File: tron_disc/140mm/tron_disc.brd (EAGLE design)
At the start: 127 x 127 mm, 75 parts, among them IC1 SLICE_NOSHIFT_TLC5947HTSSOP32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, IC2 MEGA328-AI, IC3 SLICE_NOSHIFT_TLC5947HTSSOP32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, IC4 SLICE_NOSHIFT_TLC5947HTSSOP32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, X1 16Mhz

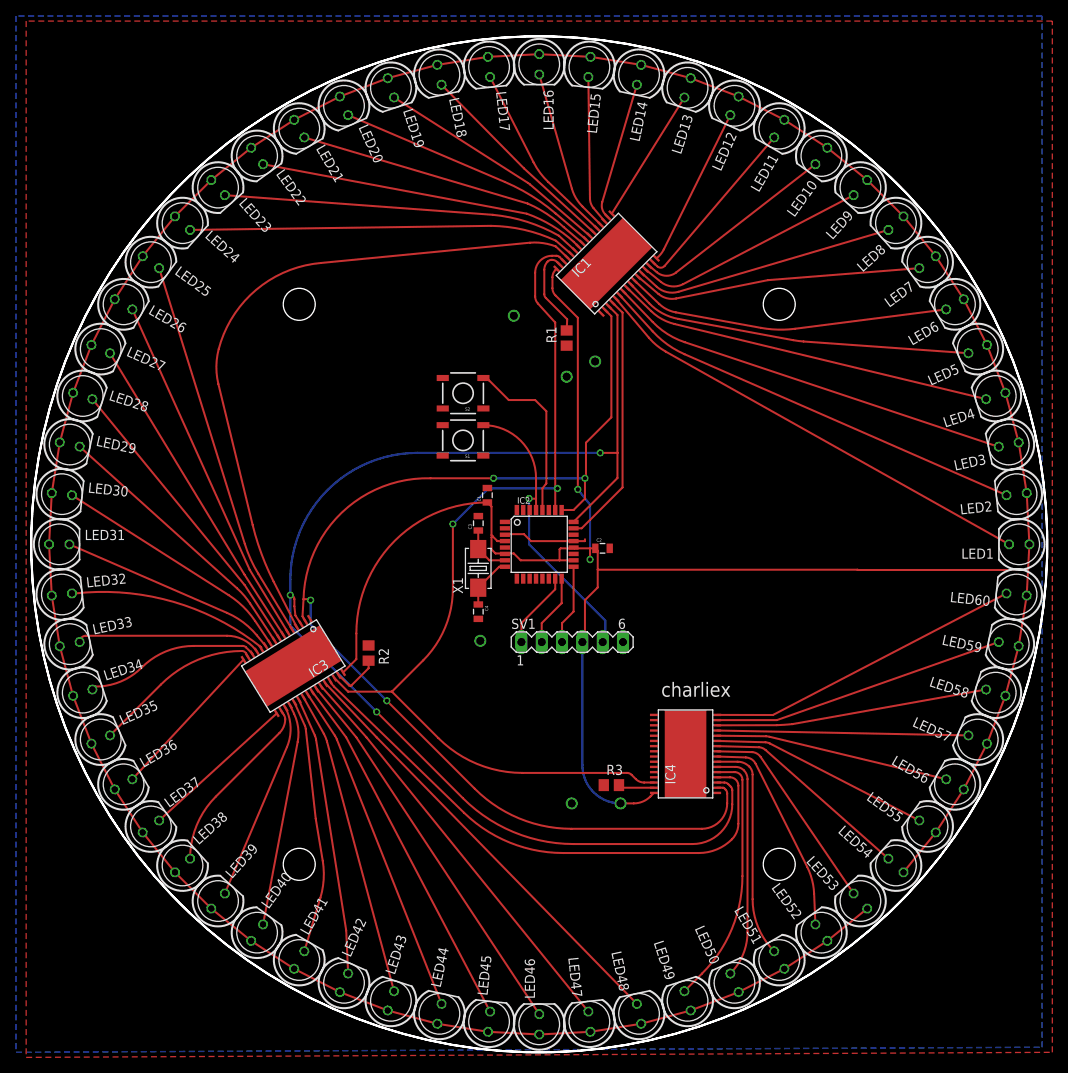
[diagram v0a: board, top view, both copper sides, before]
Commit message: 
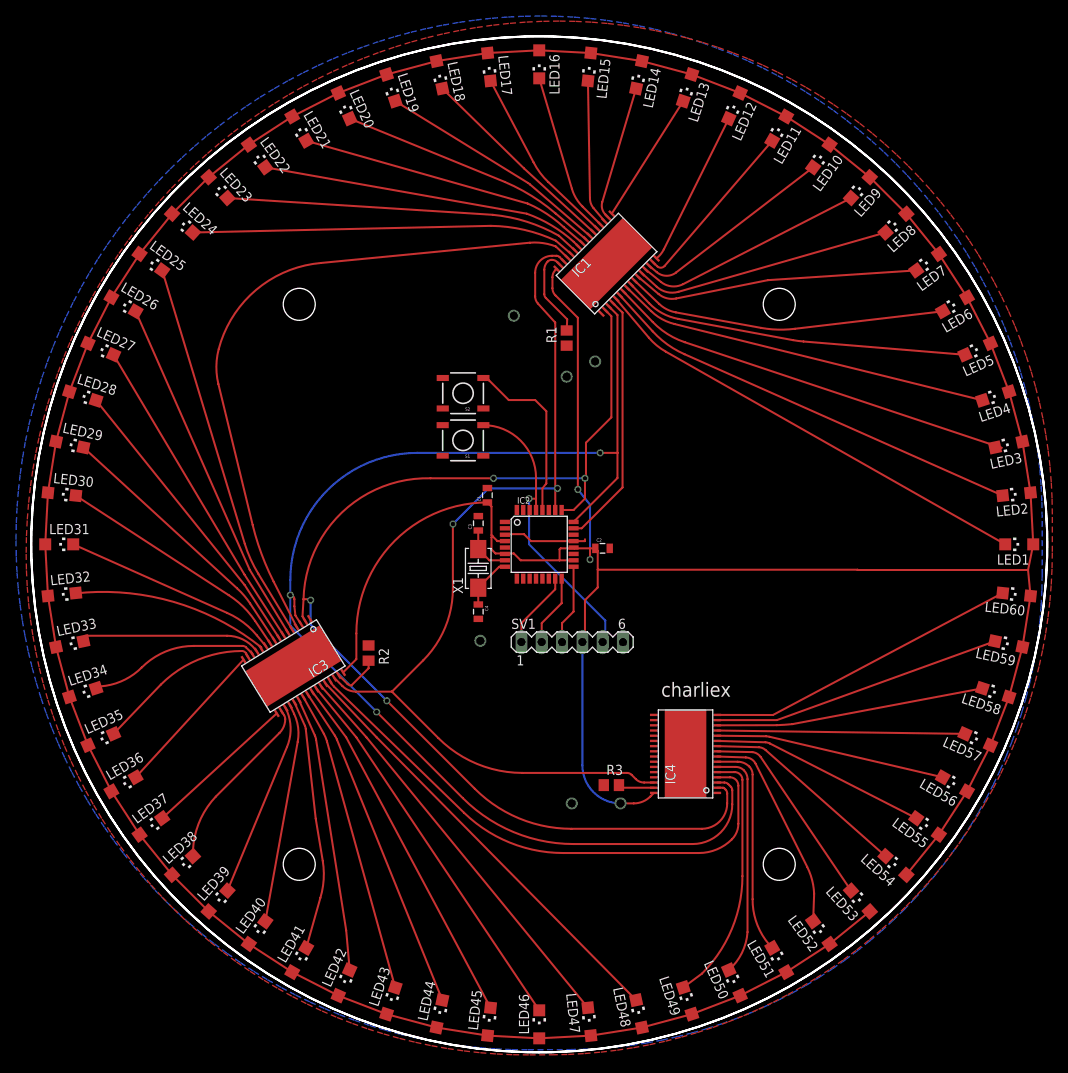
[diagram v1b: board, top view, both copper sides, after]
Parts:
- LED1, LED10, LED11, LED12, LED13, LED14, LED15, LED16, LED17, LED18, LED19, LED2, LED20, LED21, LED22, LED23, LED24, LED25, LED26, LED27, LED28, LED29, LED3, LED30, LED31, LED32, LED33, LED34, LED35, LED36, LED37, LED38, LED39, LED4, LED40, LED41, LED42, LED43, LED44, LED45, LED46, LED47, LED48, LED49, LED5, LED50, LED51, LED52, LED53, LED54, LED55, LED56, LED57, LED58, LED59, LED6, LED60, LED7, LED8, LED9: device led:LED5MM -> led:CHIPLED_1206
- turned LED1 to 90 degrees
- turned LED10 to 144 degrees
- turned LED11 to 150 degrees
- turned LED12 to 156 degrees
- turned LED13 to 162 degrees
- turned LED14 to 168 degrees
- turned LED15 to 174 degrees
- turned LED16 to 180 degrees
- turned LED17 to 186 degrees
- turned LED18 to 192 degrees
- turned LED19 to 198 degrees
- turned LED2 to 96 degrees
- turned LED20 to 204 degrees
- turned LED21 to 210 degrees
- turned LED22 to 216 degrees
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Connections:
- net COL1: now also LED1.C; no longer LED1.K
- net COL10: now also LED10.C; no longer LED10.K
- net COL11: now also LED11.C; no longer LED11.K
- net COL12: now also LED12.C; no longer LED12.K
- net COL13: now also LED13.C; no longer LED13.K
- net COL14: now also LED14.C; no longer LED14.K
- net COL15: now also LED15.C; no longer LED15.K
- net COL16: now also LED16.C; no longer LED16.K
- net COL17: now also LED17.C; no longer LED17.K
- net COL18: now also LED18.C; no longer LED18.K
- net COL19: now also LED19.C; no longer LED19.K
- net COL2: now also LED2.C; no longer LED2.K
- net COL20: now also LED20.C; no longer LED20.K
- net COL21: now also LED21.C; no longer LED21.K
- net COL22: now also LED22.C; no longer LED22.K
- net COL23: now also LED23.C; no longer LED23.K
- net COL24: now also LED24.C; no longer LED24.K
- net COL25: now also LED25.C; no longer LED25.K
- net COL26: now also LED26.C; no longer LED26.K
- net COL27: now also LED27.C; no longer LED27.K
- net COL28: now also LED28.C; no longer LED28.K
- net COL29: now also LED29.C; no longer LED29.K
- net COL3: now also LED3.C; no longer LED3.K
- net COL30: now also LED30.C; no longer LED30.K
- net COL31: now also LED31.C; no longer LED31.K
- net COL32: now also LED32.C; no longer LED32.K
- net COL33: now also LED33.C; no longer LED33.K
- net COL34: now also LED34.C; no longer LED34.K
- net COL35: now also LED35.C; no longer LED35.K
- net COL36: now also LED36.C; no longer LED36.K
- net COL37: now also LED37.C; no longer LED37.K
- net COL38: now also LED38.C; no longer LED38.K
- net COL39: now also LED39.C; no longer LED39.K
- net COL4: now also LED4.C; no longer LED4.K
- net COL40: now also LED40.C; no longer LED40.K
- net COL41: now also LED41.C; no longer LED41.K
- net COL42: now also LED42.C; no longer LED42.K
- net COL43: now also LED43.C; no longer LED43.K
- net COL44: now also LED44.C; no longer LED44.K
- net COL45: now also LED45.C; no longer LED45.K
- net COL46: now also LED46.C; no longer LED46.K
- net COL47: now also LED47.C; no longer LED47.K
- net COL48: now also LED48.C; no longer LED48.K
- net COL49: now also LED49.C; no longer LED49.K
- net COL5: now also LED5.C; no longer LED5.K
- net COL50: now also LED50.C; no longer LED50.K
- net COL51: now also LED51.C; no longer LED51.K
- net COL52: now also LED52.C; no longer LED52.K
- net COL53: now also LED53.C; no longer LED53.K
- net COL54: now also LED54.C; no longer LED54.K
- net COL55: now also LED55.C; no longer LED55.K
- net COL56: now also LED56.C; no longer LED56.K
- net COL57: now also LED57.C; no longer LED57.K
- net COL58: now also LED58.C; no longer LED58.K
- net COL59: now also LED59.C; no longer LED59.K
- net COL6: now also LED6.C; no longer LED6.K
- net COL60: now also LED60.C; no longer LED60.K
- net COL7: now also LED7.C; no longer LED7.K
- net COL8: now also LED8.C; no longer LED8.K
- net COL9: now also LED9.C; no longer LED9.K
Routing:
- net VCC: track 564.8 -> 567.8 mm
